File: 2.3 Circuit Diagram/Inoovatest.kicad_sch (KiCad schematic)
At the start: 46 parts, among them J1 USB_C Charging port, J2 USB_A, Q1 AO3400A, U1 TPS61170, U2 TPS61089, U3 TPS61099, U5 TouchScreen/SPI Touch Control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

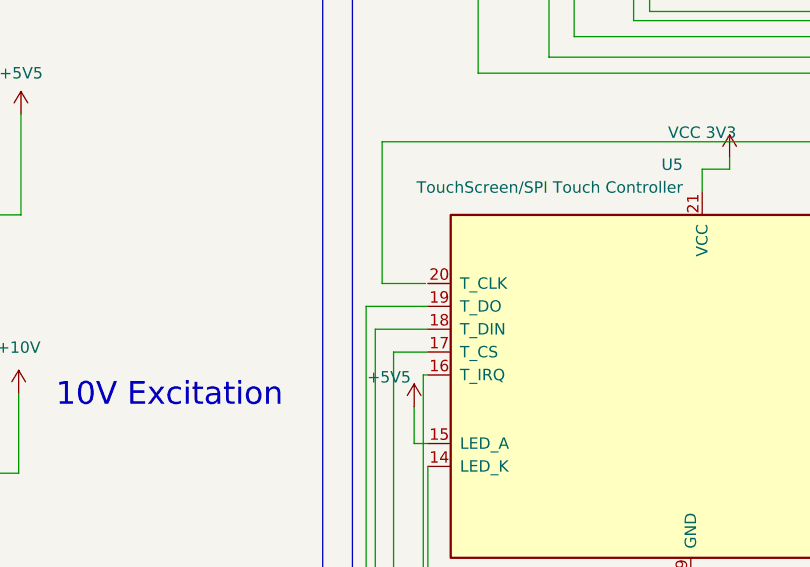
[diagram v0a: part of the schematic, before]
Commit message: Adding Measurement Chain to Schematic
- added measurement chain as well as the switching of the excitation voltages
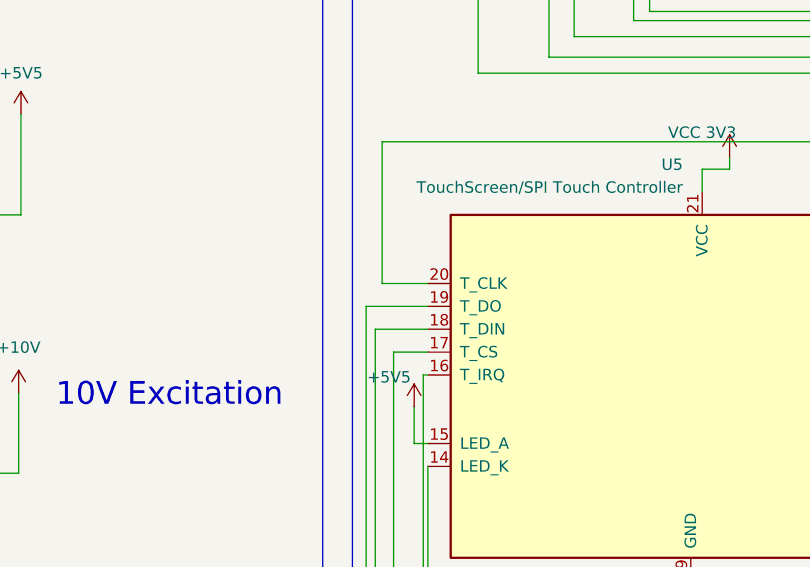
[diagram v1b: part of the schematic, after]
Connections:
- net at U4.57 (GPIO28): now also U5.20 (T_CLK)
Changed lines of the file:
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@@
 	(wire
 		(pts
-			(xy 185.928 157.988) (xy 181.102 157.988)
+			(xy 181.102 157.988) (xy 186.182 157.988)
 		)
 		(stroke
